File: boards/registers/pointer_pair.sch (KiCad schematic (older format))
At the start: 10 parts, among them U5 MC74ACT86DG, U6 SN74ACT08PW, U7 SN74ACT32PWR, U8 SN74ACT32PWR

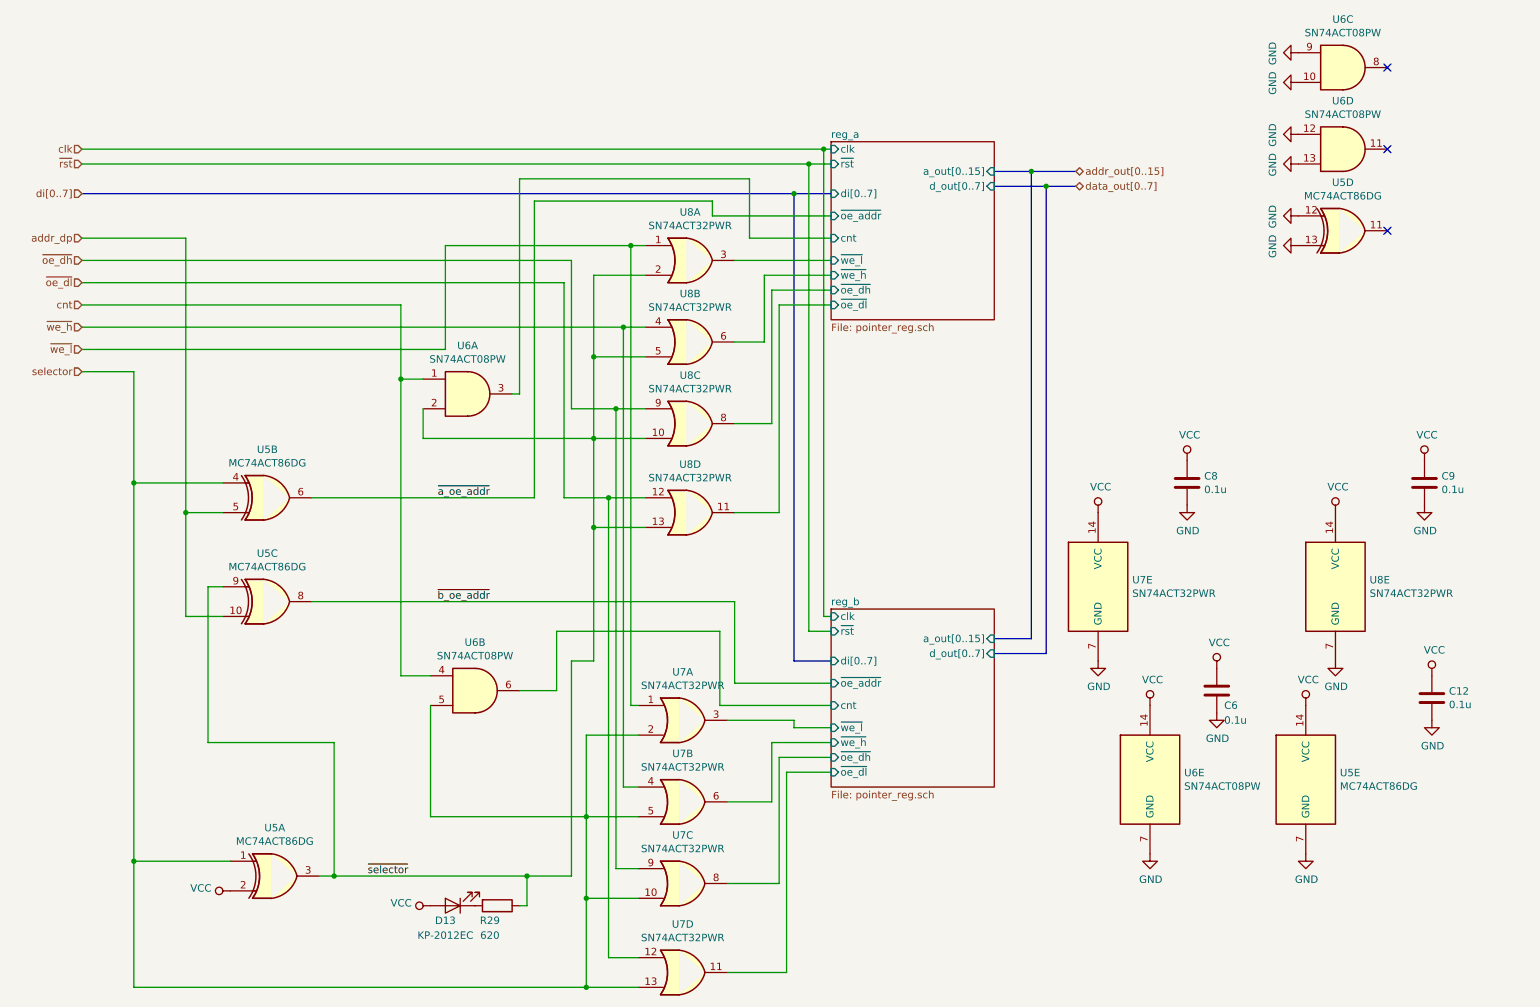
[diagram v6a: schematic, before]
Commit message: Registers: change logic family to HC and LV-A
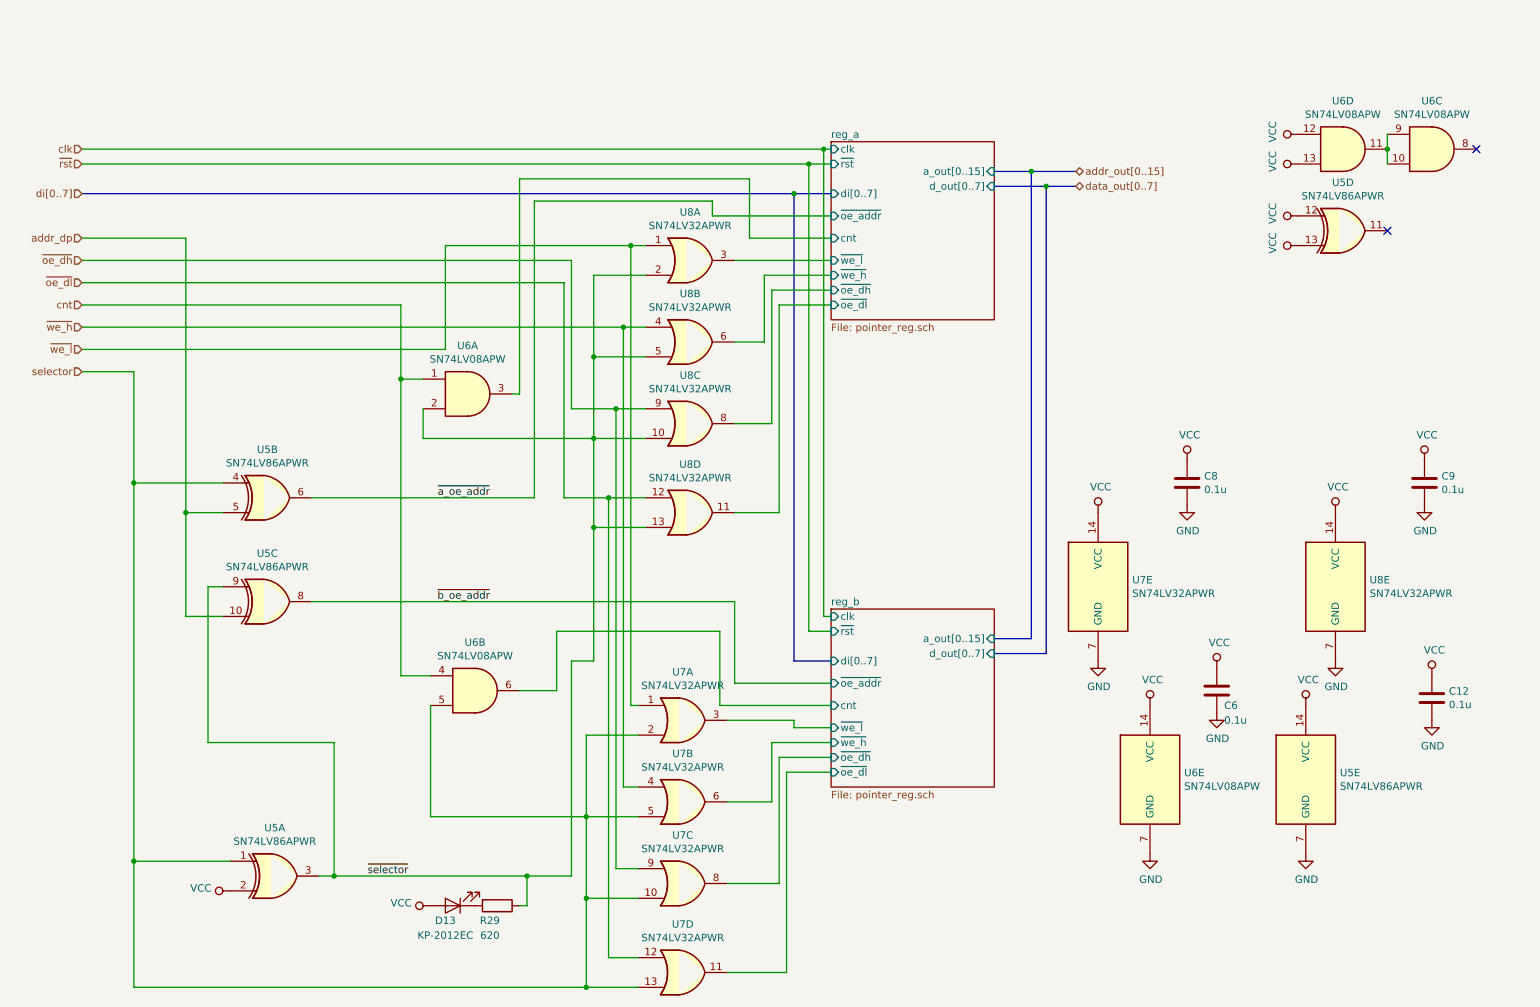
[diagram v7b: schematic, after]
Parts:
- U5: value MC74ACT86DG -> SN74LV86APWR; footprint Package_SO:SOIC-14_3.9x8.7mm_P1.27mm -> Package_SO:TSSOP-14_4.4x5mm_P0.65mm
- U6: value SN74ACT08PW -> SN74LV08APW
- U7, U8: value SN74ACT32PWR -> SN74LV32APWR
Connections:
- net GND: no longer U5.12, U5.13, U6.10, U6.12, U6.13, U6.9
- net VCC: now also U5.12, U5.13, U6.12, U6.13
- net at U6.11: now also U6.10, U6.9
- no-connect marks 3 -> 2
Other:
- moved on the sheet: U6C
